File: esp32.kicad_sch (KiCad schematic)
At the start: 19 parts, among them SW1 SW_Push, SW2 SW_Push, U4 ESP32-WROOM-32D

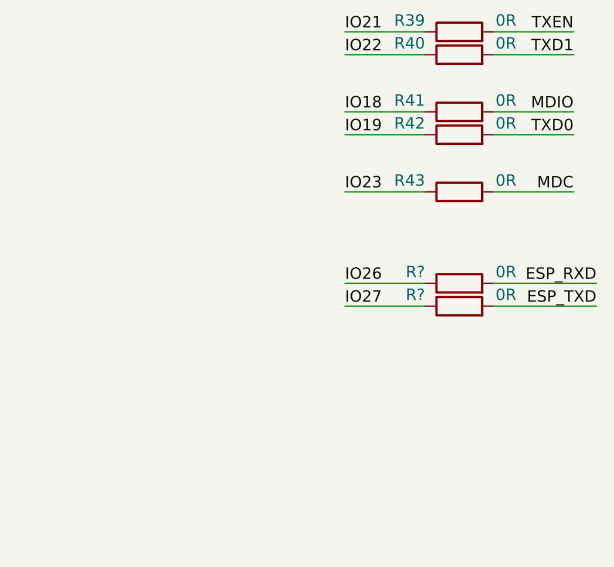
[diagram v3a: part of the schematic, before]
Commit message: Adicionado os circuitos de RxD, NEt Status, Status do módulo BG95
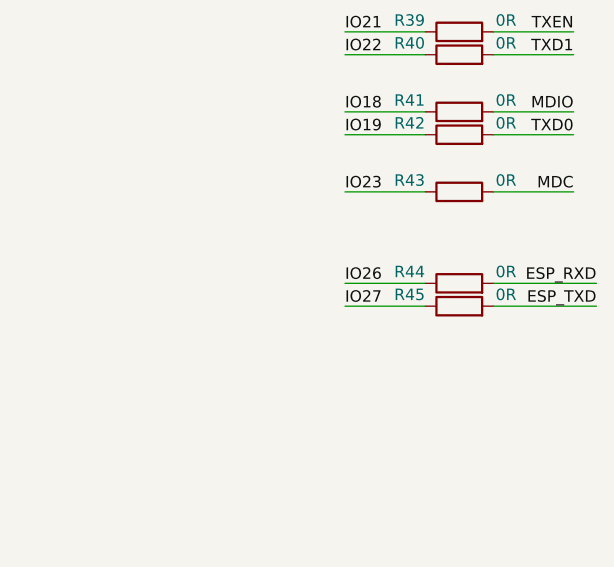
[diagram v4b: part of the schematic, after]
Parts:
- gave numbers to parts that had none: 2
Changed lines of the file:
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@@
   (symbol (lib_id "Device:R") (at 218.44 133.35 90) (unit 1)
     (in_bom yes) (on_board yes)
-    (property "Reference" "R?" (id 0) (at 214.63 132.08 90)
+    (property "Reference" "R44" (id 0) (at 214.63 132.08 90)
       (effects (font (size 1.27 1.27)) (justify left))
     )
@@
   (symbol (lib_id "Device:R") (at 218.44 135.89 90) (unit 1)
     (in_bom yes) (on_board yes)
-    (property "Reference" "R?" (id 0) (at 214.63 134.62 90)
+    (property "Reference" "R45" (id 0) (at 214.63 134.62 90)
       (effects (font (size 1.27 1.27)) (justify left))
     )

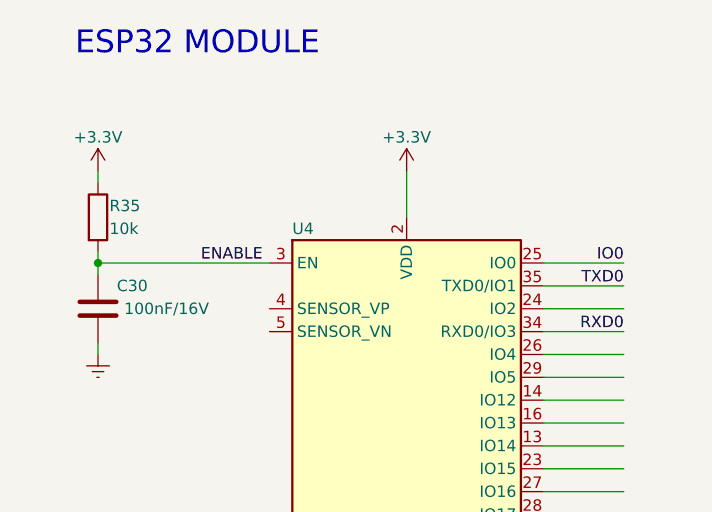
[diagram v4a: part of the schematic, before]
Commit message: Adicionado regulador 3.3V
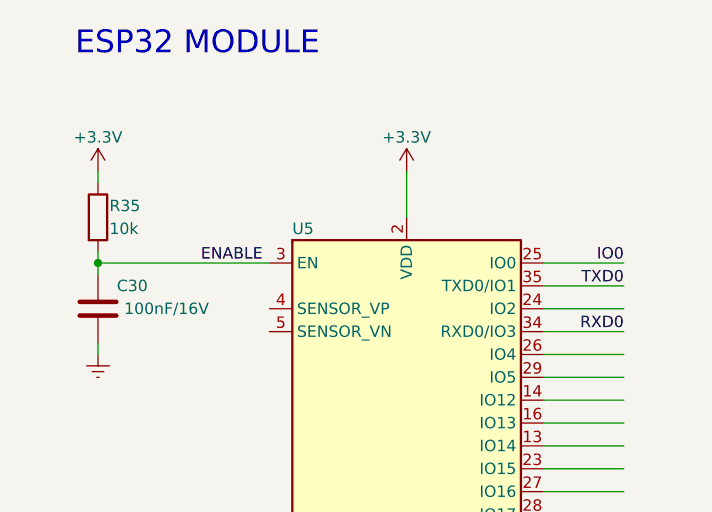
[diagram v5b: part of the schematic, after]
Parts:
- renumbered U4 to U5
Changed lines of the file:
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@@
   (symbol (lib_id "power:GNDREF") (at 62.23 181.61 0) (unit 1)
     (in_bom yes) (on_board yes) (fields_autoplaced)
-    (property "Reference" "#PWR059" (id 0) (at 62.23 187.96 0)
+    (property "Reference" "#PWR061" (id 0) (at 62.23 187.96 0)
       (effects (font (size 1.27 1.27)) hide)
     )
@@
   (symbol (lib_id "power:+3.3V") (at 50.8 41.91 0) (unit 1)
     (in_bom yes) (on_board yes)
-    (property "Reference" "#PWR053" (id 0) (at 50.8 45.72 0)
+    (property "Reference" "#PWR055" (id 0) (at 50.8 45.72 0)
       (effects (font (size 1.27 1.27)) hide)
     )
@@
   (symbol (lib_id "RF_Module:ESP32-WROOM-32D") (at 85.09 82.55 0) (unit 1)
     (in_bom yes) (on_board yes)
-    (property "Reference" "U4" (id 0) (at 72.39 48.26 0)
+    (property "Reference" "U5" (id 0) (at 72.39 48.26 0)
       (effects (font (size 1.27 1.27)) (justify left))
     )
@@
   (symbol (lib_id "power:+3.3V") (at 218.44 49.53 0) (unit 1)
     (in_bom yes) (on_board yes)
-    (property "Reference" "#PWR055" (id 0) (at 218.44 53.34 0)
+    (property "Reference" "#PWR057" (id 0) (at 218.44 53.34 0)
       (effects (font (size 1.27 1.27)) hide)
     )
@@
   (symbol (lib_id "power:GNDREF") (at 96.52 181.61 0) (unit 1)
     (in_bom yes) (on_board yes) (fields_autoplaced)
-    (property "Reference" "#PWR060" (id 0) (at 96.52 187.96 0)
+    (property "Reference" "#PWR062" (id 0) (at 96.52 187.96 0)
       (effects (font (size 1.27 1.27)) hide)
     )
@@
   (symbol (lib_id "power:GNDREF") (at 50.8 62.23 0) (unit 1)
     (in_bom yes) (on_board yes) (fields_autoplaced)
-    (property "Reference" "#PWR056" (id 0) (at 50.8 68.58 0)
+    (property "Reference" "#PWR058" (id 0) (at 50.8 68.58 0)
       (effects (font (size 1.27 1.27)) hide)
     )
@@
   (symbol (lib_id "power:GNDREF") (at 218.44 62.23 0) (unit 1)
     (in_bom yes) (on_board yes) (fields_autoplaced)
-    (property "Reference" "#PWR057" (id 0) (at 218.44 68.58 0)
+    (property "Reference" "#PWR059" (id 0) (at 218.44 68.58 0)
       (effects (font (size 1.27 1.27)) hide)
     )
@@
   (symbol (lib_id "power:+3.3V") (at 85.09 41.91 0) (unit 1)
     (in_bom yes) (on_board yes)
-    (property "Reference" "#PWR054" (id 0) (at 85.09 45.72 0)
+    (property "Reference" "#PWR056" (id 0) (at 85.09 45.72 0)
       (effects (font (size 1.27 1.27)) hide)
     )
@@
   (symbol (lib_id "power:GNDREF") (at 85.09 120.65 0) (unit 1)
     (in_bom yes) (on_board yes) (fields_autoplaced)
-    (property "Reference" "#PWR058" (id 0) (at 85.09 127 0)
-      (effects (font (size 1.27 1.27)) hide)
-    )
+    (property "Reference" "#PWR060" (id 0) (at 85.09 127 0)
+      (effects (font (size 1.27 1.27)) hide)
+    )

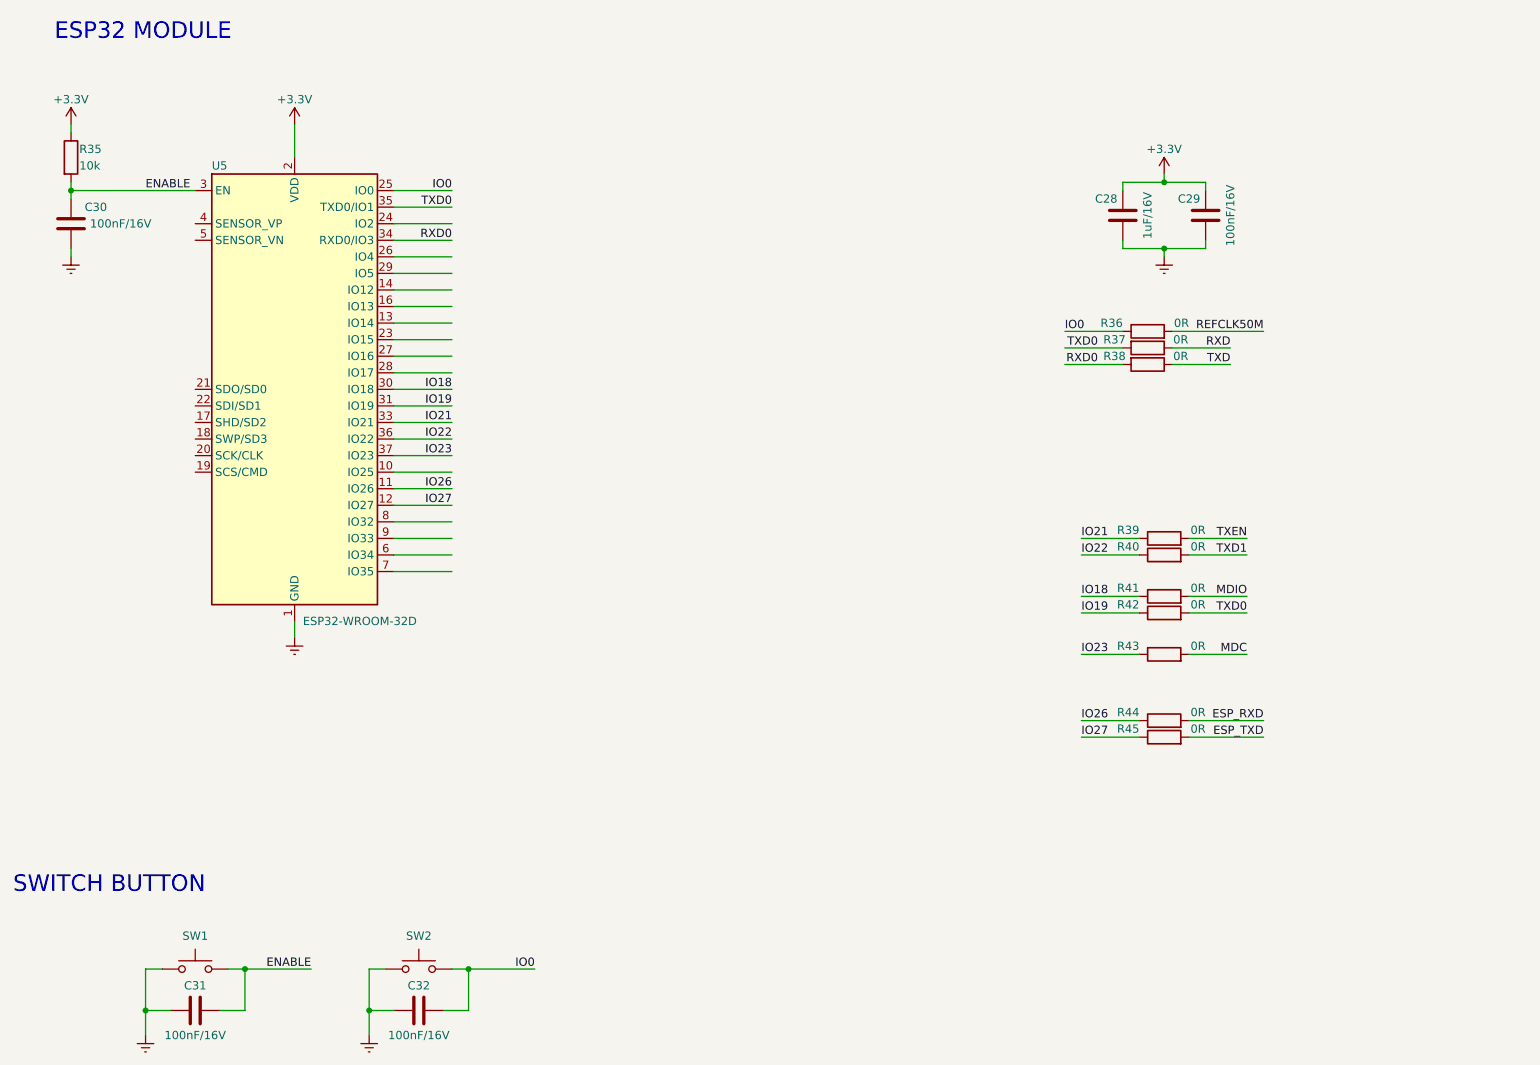
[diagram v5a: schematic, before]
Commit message: Adicionado hierarchical label
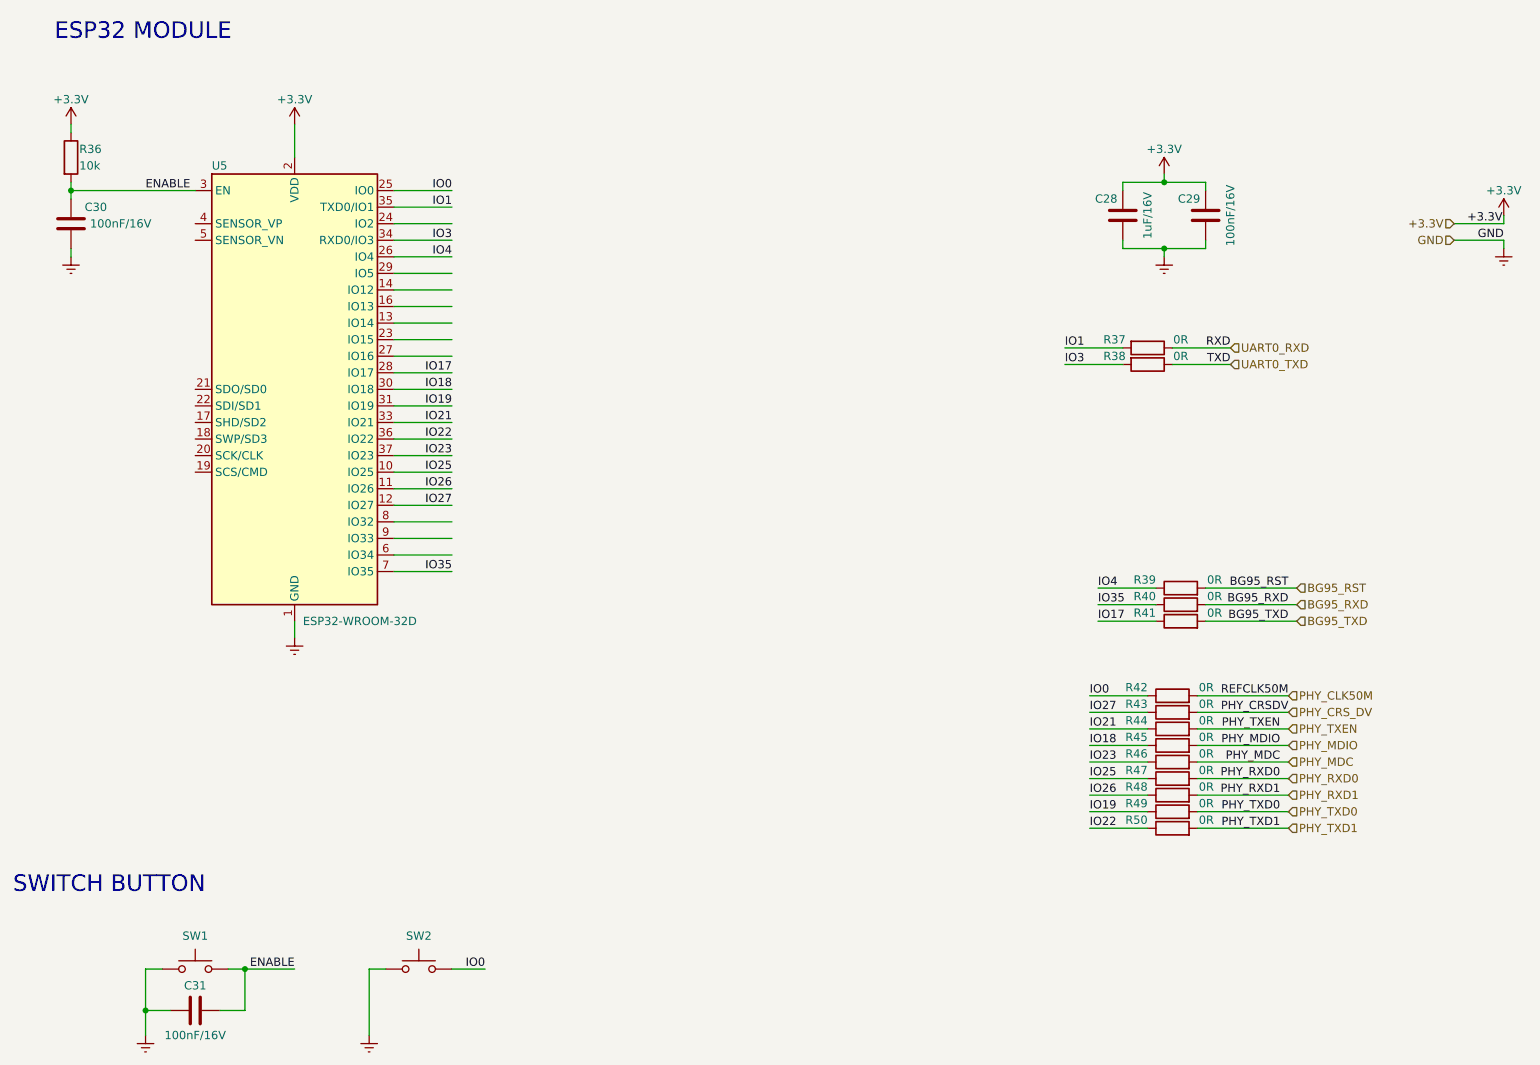
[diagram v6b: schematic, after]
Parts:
- removed C32: 100nF/16V, Capacitor_SMD:C_0402_1005Metric_Pad0.74x0.62mm_HandSolder, symbol Device:C
- added R39, R43, R47, R48: 0R, Resistor_SMD:R_0402_1005Metric_Pad0.72x0.64mm_HandSolder, symbol Device:R
- renumbered R35 to R36, R44 to R40, R45 to R41, R36 to R42, R39 to R44, R41 to R45, R43 to R46, R42 to R49, R40 to R50
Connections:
- net IO26: now also R48.1; no longer R40.1
- net IO27: now also R43.1; no longer R41.1
- net IO25: now reaches U5.10 (IO25)
- net IO25: now also R47.1
- net IO4: now reaches U5.26 (IO4)
- net IO4: now also R39.1
- net IO17: now reaches U5.28 (IO17)
- net IO17: now also R41.1
- net IO35: now reaches U5.7 (IO35)
- net IO35: now also R40.1
- net ESP_RXD renamed BG95_RXD
- net ESP_TXD renamed BG95_TXD
- net MDC renamed PHY_MDC
- net MDIO renamed PHY_MDIO
- net REFCLK50M renamed PHY_CLK50M
- net RXD renamed UART0_RXD
- net RXD0 renamed IO3
- net TXD renamed UART0_TXD
- net TXD0 renamed IO1
- net IO1: no longer R49.2
- net TXD1 renamed PHY_TXD1
- net TXEN renamed PHY_TXEN
- new net BG95_RST: R39.2
- new net PHY_CRS_DV: R43.2
- new net PHY_RXD0: R47.2
- new net PHY_RXD1: R48.2
- new net PHY_TXD0: R49.2
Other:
- moved on the sheet: R40, R41, R42, R44, R45, R46, R49, R50

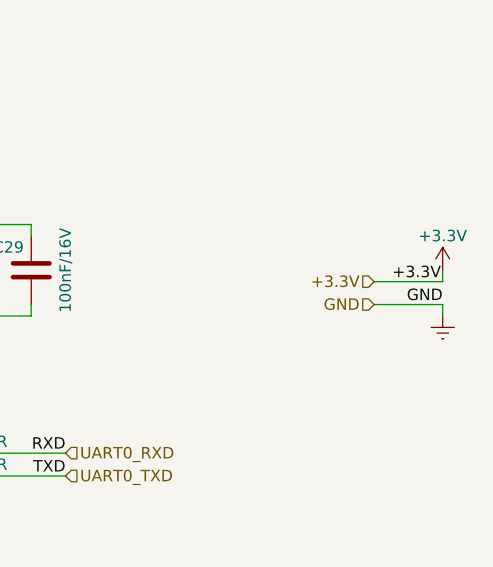
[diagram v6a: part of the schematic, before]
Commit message: Cont. hierarchical label e descrição das folhas
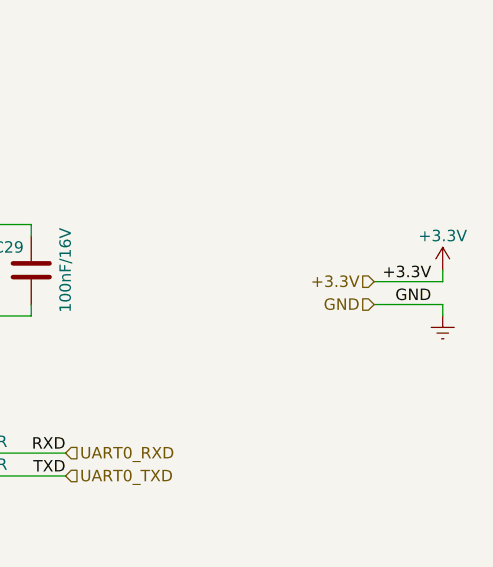
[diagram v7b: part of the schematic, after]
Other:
- company: (none) -> Magalhaes
- title: (none) -> ESP32-WROOM-32D
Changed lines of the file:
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@@
   (paper "A4")
   (title_block
+    (title "ESP32-WROOM-32D")
     (date "2022-06-24")
+    (rev "0.0.0")
+    (company "Magalhaes")
+    (comment 1 "Author: Alexandre Magalhães")
+    (comment 2 "Variant 1: Full")
   )
   (junction (at 218.44 60.96) (diameter 0) (color 0 0 0 0)
@@
     (stroke (width 0) (type default) (color 0 0 0 0))
   )
+  (wire (pts (xy 270.51 59.69) (xy 270.51 60.96))
+    (stroke (width 0) (type default) (color 0 0 0 0))
+  )
   (wire (pts (xy 85.09 41.91) (xy 85.09 46.99))
     (stroke (width 0) (type default) (color 0 0 0 0))
@@
     (stroke (width 0) (type default) (color 0 0 0 0))
   )
+  (wire (pts (xy 262.89 59.69) (xy 270.51 59.69))
+    (stroke (width 0) (type default) (color 0 0 0 0))
+  )
   (wire (pts (xy 77.47 171.45) (xy 85.09 171.45))
     (stroke (width 0) (type default) (color 0 0 0 0))
@@
     (stroke (width 0) (type default) (color 0 0 0 0))
   )
+  (wire (pts (xy 270.51 57.15) (xy 270.51 55.88))
+    (stroke (width 0) (type default) (color 0 0 0 0))
+  )
   (wire (pts (xy 207.01 149.86) (xy 215.9 149.86))
     (stroke (width 0) (type default) (color 0 0 0 0))
@@
     (stroke (width 0) (type default) (color 0 0 0 0))
   )
+  (wire (pts (xy 262.89 57.15) (xy 270.51 57.15))
+    (stroke (width 0) (type default) (color 0 0 0 0))
+  )
   (wire (pts (xy 223.52 132.08) (xy 237.49 132.08))
     (stroke (width 0) (type default) (color 0 0 0 0))
   )
-  (wire (pts (xy 262.89 59.69) (xy 270.51 59.69))
-    (stroke (width 0) (type default) (color 0 0 0 0))
-  )
-  (wire (pts (xy 270.51 55.88) (xy 270.51 57.15))
-    (stroke (width 0) (type default) (color 0 0 0 0))
-  )
   (wire (pts (xy 224.79 59.69) (xy 224.79 60.96))
     (stroke (width 0) (type default) (color 0 0 0 0))
   )
-  (wire (pts (xy 270.51 59.69) (xy 270.51 60.96))
-    (stroke (width 0) (type default) (color 0 0 0 0))
-  )
   (wire (pts (xy 50.8 60.96) (xy 50.8 62.23))
     (stroke (width 0) (type default) (color 0 0 0 0))
@@
   )
   (wire (pts (xy 100.33 82.55) (xy 109.22 82.55))
-    (stroke (width 0) (type default) (color 0 0 0 0))
-  )
-  (wire (pts (xy 262.89 57.15) (xy 270.51 57.15))
     (stroke (width 0) (type default) (color 0 0 0 0))
   )
@@
     (effects (font (size 1.27 1.27)) (justify left bottom))
   )
-  (label "GND" (at 270.51 59.69 180)
+  (label "GND" (at 269.24 59.69 180)
     (effects (font (size 1.27 1.27)) (justify right bottom))
   )
@@
     (effects (font (size 1.27 1.27)) (justify right bottom))
   )
-  (label "+3.3V" (at 270.3216 57.15 180)
-    (effects (font (size 1.27 1.27)) (justify right bottom))
-  )
+  (label "+3.3V" (at 269.24 57.15 180)
+    (effects (font (size 1.27 1.27)) (justify right bottom))
+  )
